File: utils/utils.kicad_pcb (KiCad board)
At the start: 2 copper layers, 35 x 70.5 mm, 35 parts, among them J1 AIN, J2 BIN, J3 GATE, J4 EURORACK_CONN_10, J5 ~OUT, J6 OUT, J7 Conn_01x04, J8 Conn_01x05, J9 Conn_01x03_Male, Q1 2N3904, U1 TL072, U2 4066, U3 LM317L_TO92, U4 LM337L_TO92

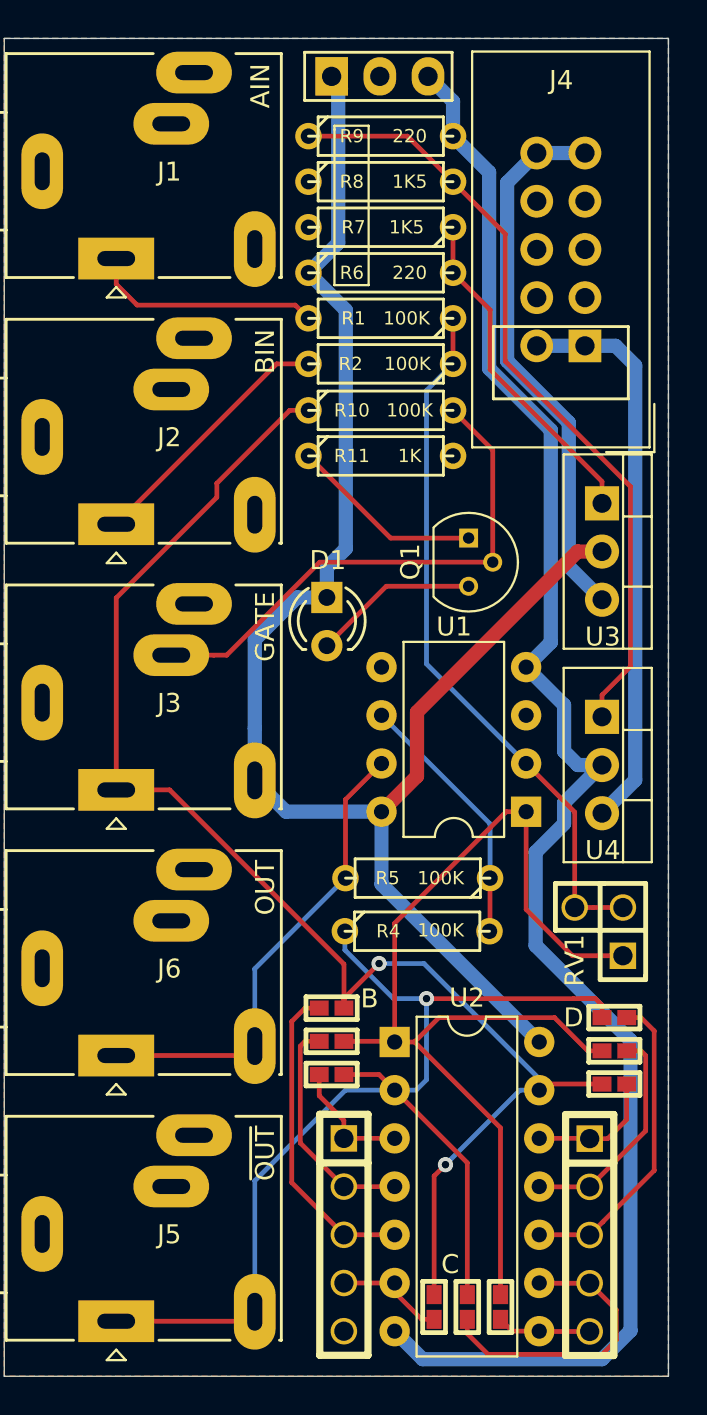
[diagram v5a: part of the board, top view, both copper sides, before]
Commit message: add support for fixed CV output when no input
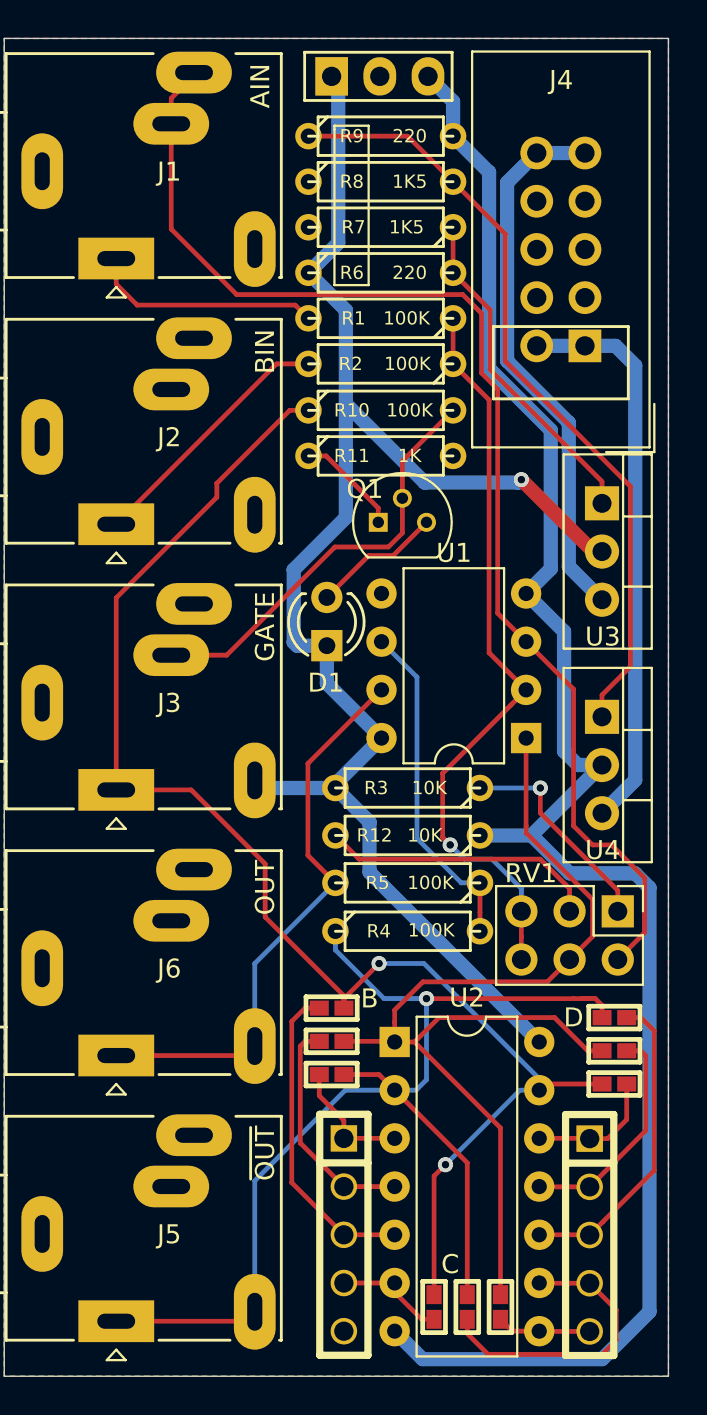
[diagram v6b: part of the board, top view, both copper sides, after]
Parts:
- added R12: 10K, 4ms/4ms-kicad-lib/4ms-footprints.pretty:Resistor_TH_300, F.Cu at (144.3, 85.0)
- added R3: 10K, 4ms/4ms-kicad-lib/4ms-footprints.pretty:Resistor_TH_300, F.Cu at (144.3, 82.5)
- RV1: footprint imciner2/KiCad-Libraries/modules/Connectors.pretty:CONN_2.54mm_1x03 -> 4ms/4ms-kicad-lib/4ms-footprints.pretty:Pin_Header_Straight_2x03_Pitch2.54mm
- moved Q1 4.07 mm to (144.0, 68.5), turned to 0 degrees
- moved U1 3.88 mm to (150.5, 79.9)
- moved RV1 3.17 mm to (152.8, 90.3)
- moved R5 0.59 mm to (144.3, 87.5)
- moved R4 0.50 mm to (144.3, 90.0)
- turned D1 to 270 degrees
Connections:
- J1 pad S: GND -> A_CONN
- J1 pad SN: GND -> A_CONN
- RV1 pad 1: STAGE1_OUT -> Net-(R3-Pad1)
- RV1 pad 2: Net-(R1-Pad1) -> A_CONN
- RV1 pad 3: Net-(R1-Pad1) -> Net-(R12-Pad2)
- U1 pad 3: GND -> A_CONN
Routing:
- net A_CONN: track 0.00 -> 65.7 mm
- net Net-(R12-Pad2): track 0.00 -> 14.7 mm
- net Net-(R3-Pad1): track 0.00 -> 11.4 mm, vias 0 -> 1
- net -10V: track 89.5 -> 95.2 mm
- net GATE_CONN: track 27.8 -> 22.4 mm
- net Net-(Q1-Pad1): track 10.2 -> 5.57 mm
- net OUT: track 25.6 -> 30.2 mm
- net Net-(R4-Pad2): track 13.7 -> 18.0 mm
- net Net-(R1-Pad1): track 37.4 -> 40.0 mm, vias 0 -> 1
- net Net-(D1-Pad1): track 8.77 -> 6.89 mm
- net +10V: track 86.3 -> 84.8 mm, vias 0 -> 1
- net STAGE1_OUT: track 56.9 -> 55.7 mm
- net GATE: track 74.2 -> 74.8 mm
- net ~OUT: track 62.3 -> 62.8 mm

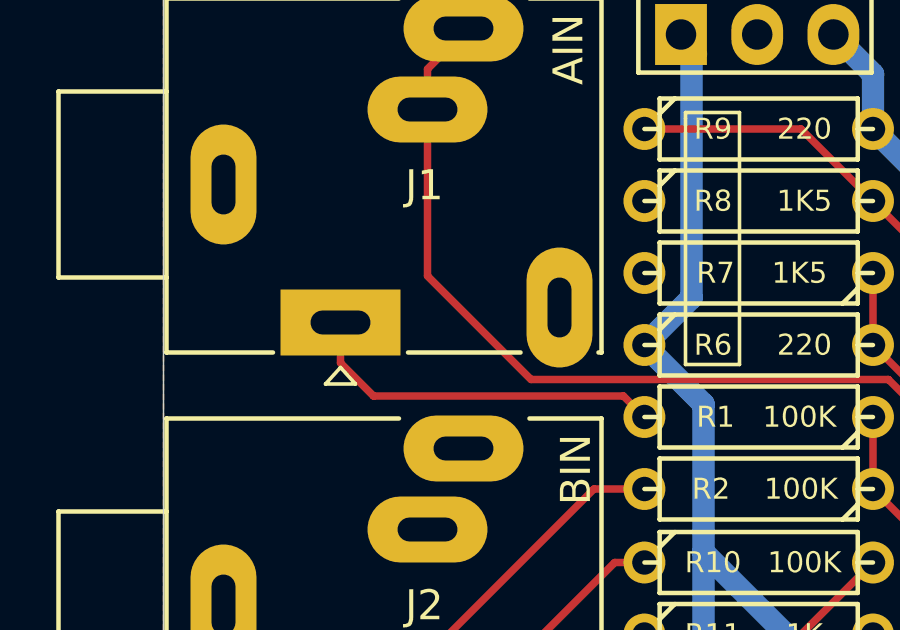
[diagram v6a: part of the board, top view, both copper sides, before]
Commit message: correction based on breadboard test
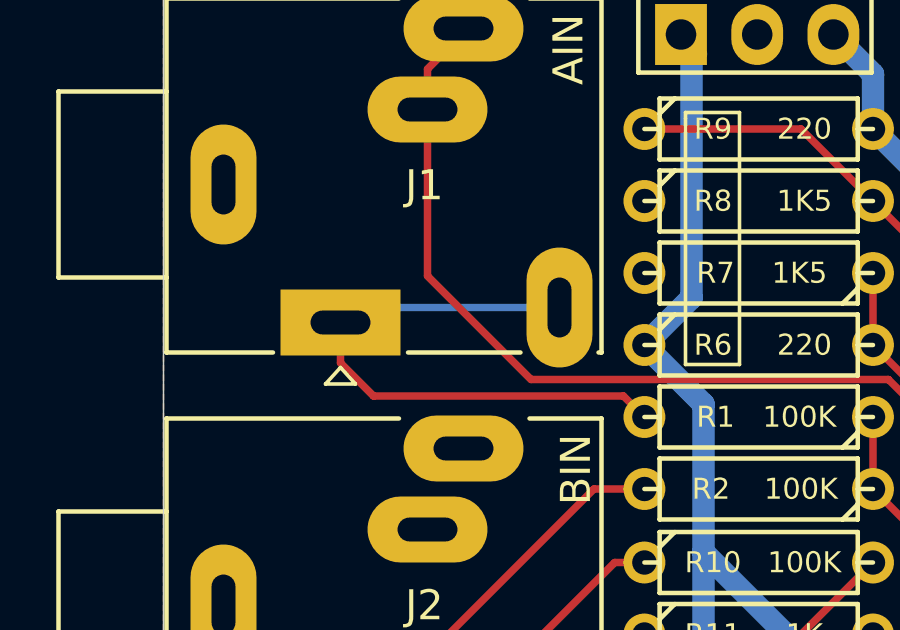
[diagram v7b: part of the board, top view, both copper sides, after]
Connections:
- J1 pad TN: GND -> AIN
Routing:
- net AIN: track 12.2 -> 19.7 mm
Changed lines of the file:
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@@
     (thickness 1.6)
     (drawings 14)
-    (tracks 267)
+    (tracks 269)
     (zones 0)
     (modules 37)
@@
   )
   (setup
-    (last_trace_width 0.75)
+    (last_trace_width 0.25)
     (user_trace_width 0.75)
     (trace_clearance 0.2)
@@
       (net 28 A_CONN))
     (pad TN thru_hole oval (at 7.3 -0.5 90) (size 4 2.2) (drill oval 2 0.8) (layers *.Cu *.Mask)
-      (net 1 GND))
+      (net 2 AIN))
     (pad T thru_hole rect (at 0 0) (size 4 2.2) (drill oval 2 0.8) (layers *.Cu *.Mask)
       (net 2 AIN))
@@
   (segment (start 138.331501 57.051501) (end 130.001501 57.051501) (width 0.25) (layer F.Cu) (net 2))
   (segment (start 139.03 57.75) (end 138.331501 57.051501) (width 0.25) (layer F.Cu) (net 2))
+  (segment (start 129.4 54.1) (end 128.9 54.6) (width 0.25) (layer B.Cu) (net 2))
+  (segment (start 136.2 54.1) (end 129.4 54.1) (width 0.25) (layer B.Cu) (net 2))
   (segment (start 137.35 60.15) (end 128.9 68.6) (width 0.25) (layer F.Cu) (net 3))
   (segment (start 139.03 60.15) (end 137.35 60.15) (width 0.25) (layer F.Cu) (net 3))

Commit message: cleanup
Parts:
- J1: value AIN -> A_IN
- J2: value BIN -> B_IN
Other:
- board size 35 x 70.5 mm -> 34.8 x 70.5 mm
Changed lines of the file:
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@@
     (descr "TO-92 leads molded, narrow, drill 0.6mm (see NXP sot054_po.pdf)")
     (tags "to-92 sc-43 sc-43a sot54 PA33 transistor")
-    (fp_text reference Q1 (at -1.98 -1.75) (layer F.SilkS)
+    (fp_text reference Q1 (at -3.73 0) (layer F.SilkS)
       (effects (font (size 1 1) (thickness 0.15)))
     )
@@
       (effects (font (size 0.7 0.7) (thickness 0.1)))
     )
-    (fp_text value 10K (at -0.9 0) (layer F.SilkS)
+    (fp_text value 10K (at -1.15 0) (layer F.SilkS)
       (effects (font (size 0.7 0.7) (thickness 0.1)))
     )
@@
       (effects (font (size 0.7 0.7) (thickness 0.1)))
     )
-    (fp_text value 10K (at -1.14 0) (layer F.SilkS)
+    (fp_text value 10K (at -1.15 0) (layer F.SilkS)
       (effects (font (size 0.7 0.7) (thickness 0.1)))
     )
@@
     (descr "8-lead though-hole mounted DIP package, row spacing 7.62 mm (300 mils)")
     (tags "THT DIP DIL PDIP 2.54mm 7.62mm 300mil")
-    (fp_text reference U1 (at 3.8 9.75) (layer F.SilkS)
+    (fp_text reference U1 (at 3.75 0.62 180) (layer F.SilkS)
       (effects (font (size 1 1) (thickness 0.15)))
     )
@@
     (fp_line (start 8.7 9.15) (end 8.7 -1.55) (layer F.CrtYd) (width 0.05))
     (fp_line (start 8.7 -1.55) (end -1.1 -1.55) (layer F.CrtYd) (width 0.05))
-    (fp_text user %R (at 3.81 3.81) (layer F.Fab)
+    (fp_text user %R (at 3.75 0.62) (layer F.Fab)
       (effects (font (size 1 1) (thickness 0.15)))
     )
@@
       (effects (font (size 1 1) (thickness 0.15)))
     )
-    (fp_text value GATE (at 7.85 -8.6 90) (layer F.SilkS)
+    (fp_text value GATE (at 7.6 -8.6 90) (layer F.SilkS)
       (effects (font (size 1 1) (thickness 0.15)))
     )
@@
     (descr "14-lead though-hole mounted DIP package, row spacing 7.62 mm (300 mils)")
     (tags "THT DIP DIL PDIP 2.54mm 7.62mm 300mil")
-    (fp_text reference U2 (at 3.81 -2.33) (layer F.SilkS)
+    (fp_text reference U2 (at 3.81 0.616) (layer F.SilkS)
       (effects (font (size 1 1) (thickness 0.15)))
     )
@@
       (effects (font (size 1 1) (thickness 0.15)))
     )
-    (fp_text value AIN (at 7.6 -9.1 90) (layer F.SilkS)
+    (fp_text value A_IN (at 7.6 -8.85 90) (layer F.SilkS)
       (effects (font (size 1 1) (thickness 0.15)))
     )
@@
       (effects (font (size 1 1) (thickness 0.15)))
     )
-    (fp_text value BIN (at 7.85 -9.1 270) (layer F.SilkS)
+    (fp_text value B_IN (at 7.6 -8.85 270) (layer F.SilkS)
       (effects (font (size 1 1) (thickness 0.15)))
     )
@@
       (effects (font (size 1 1) (thickness 0.15)))
     )
-    (fp_text value ~OUT (at 7.85 -8.85 90) (layer F.SilkS)
+    (fp_text value ~OUT (at 7.6 -8.85 90) (layer F.SilkS)
       (effects (font (size 1 1) (thickness 0.15)))
     )
@@
       (effects (font (size 1 1) (thickness 0.15)))
     )
-    (fp_text value OUT (at 7.85 -8.85 90) (layer F.SilkS)
+    (fp_text value OUT (at 7.6 -8.85 90) (layer F.SilkS)
       (effects (font (size 1 1) (thickness 0.15)))
     )
@@
     (effects (font (size 1 1) (thickness 0.15)))
   )
-  (gr_text C (at 146.5 107.6) (layer F.SilkS)
+  (gr_text C (at 145.75 107.5) (layer F.SilkS)
     (effects (font (size 1 1) (thickness 0.15)))
   )
-  (gr_text B (at 142.25 93.6) (layer F.SilkS)
+  (gr_text B (at 138.25 94.25) (layer F.SilkS)
     (effects (font (size 1 1) (thickness 0.15)))
   )
-  (gr_text https://rabid.audio (at 155.75 54.5 90) (layer B.SilkS)
+  (gr_text https://rabid.audio (at 156.25 54.5 90) (layer B.SilkS)
     (effects (font (size 1.5 1.5) (thickness 0.15)) (justify mirror))
   )
@@
     (effects (font (size 1 1) (thickness 0.15)) (justify mirror))
   )
-  (gr_line (start 123 113.5) (end 123 43) (layer Edge.Cuts) (width 0.05))
-  (gr_line (start 158 113.5) (end 123 113.5) (layer Edge.Cuts) (width 0.05))
-  (gr_line (start 123 43) (end 158 43) (layer Edge.Cuts) (width 0.05))
+  (gr_line (start 123.25 113.5) (end 123.25 43) (layer Edge.Cuts) (width 0.05))
+  (gr_line (start 158 113.5) (end 123.25 113.5) (layer Edge.Cuts) (width 0.05))
+  (gr_line (start 123.25 43) (end 158 43) (layer Edge.Cuts) (width 0.05))
   (segment (start 128.9 55.95) (end 128.9 54.6) (width 0.25) (layer F.Cu) (net 2))
   (segment (start 130.001501 57.051501) (end 128.9 55.95) (width 0.25) (layer F.Cu) (net 2))
@@
     (polygon
       (pts
-        (xy 158 113.5) (xy 123 113.5) (xy 123 43) (xy 158 43)
+        (xy 158 113.5) (xy 123.25 113.5) (xy 123.25 43) (xy 158 43)
       )
     )
@@
     (polygon
       (pts
-        (xy 158 113.5) (xy 123 113.5) (xy 123 43) (xy 158 43)
+        (xy 158 113.5) (xy 123.25 113.5) (xy 123.25 43) (xy 158 43)
       )
     )
